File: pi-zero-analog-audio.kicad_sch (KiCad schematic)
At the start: 25 parts, among them J1 GPIO, J2 SJ1-3555NG-BE, J3 Screw_Terminal_01x04, U1 LP5907MFX-3.3, U2 74LVC2G34, U3 PAM8403D

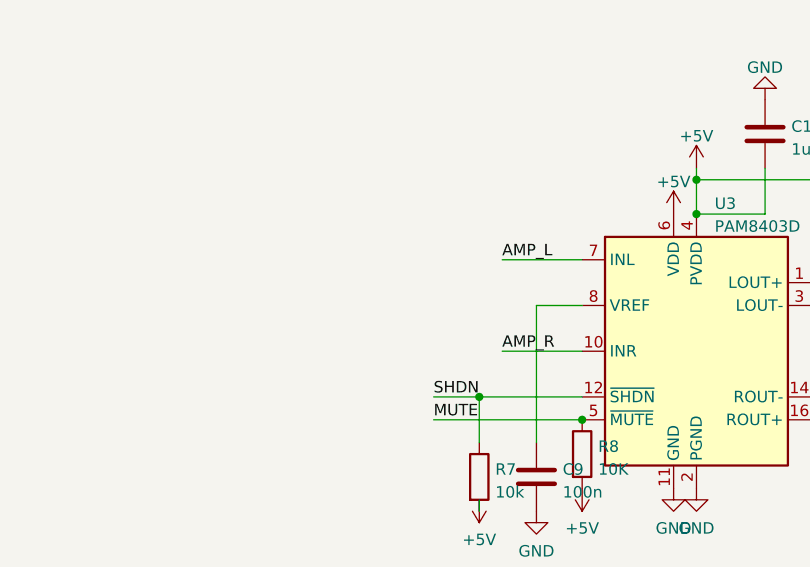
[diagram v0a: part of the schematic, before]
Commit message: Capacitor and resistor on the amplifier input, as per PAM8403 specs
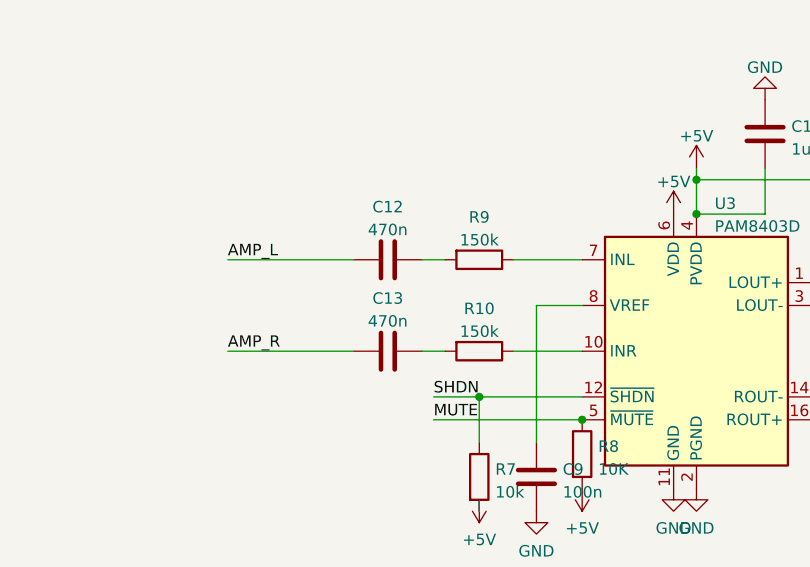
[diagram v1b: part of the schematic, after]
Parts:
- added C12, C13: 470n, Capacitor_SMD:C_0805_2012Metric_Pad1.18x1.45mm_HandSolder, symbol Device:C
- added R10, R9: 150k, Resistor_SMD:R_0805_2012Metric_Pad1.20x1.40mm_HandSolder, symbol Device:R
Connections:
- net AMP_L: now also C12.2; no longer U3.7 (INL)
- net AMP_R: now also C13.2; no longer U3.10 (INR)
- new net: R10.1, U3.10 (INR)
- new net: R9.1, U3.7 (INL)
- new net: C12.1, R9.2
- new net: C13.1, R10.2
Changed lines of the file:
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@@
+    (stroke (width 0) (type default) (color 0 0 0 0))
+  )
+  (wire (pts (xy 97.79 107.95) (xy 100.33 107.95))
     (stroke (width 0) (type default) (color 0 0 0 0))
   )
@@
     (stroke (width 0) (type default) (color 0 0 0 0))
   )
+  (wire (pts (xy 76.2 118.11) (xy 90.17 118.11))
+    (stroke (width 0) (type default) (color 0 0 0 0))
+  )
   (wire (pts (xy 40.64 64.77) (xy 38.1 64.77))
     (stroke (width 0) (type solid) (color 0 0 0 0))
@@
     (stroke (width 0) (type default) (color 0 0 0 0))
   )
+  (wire (pts (xy 97.79 118.11) (xy 100.33 118.11))
+    (stroke (width 0) (type default) (color 0 0 0 0))
+  )
   (wire (pts (xy 40.64 26.67) (xy 38.1 26.67))
     (stroke (width 0) (type solid) (color 0 0 0 0))
@@
     (stroke (width 0) (type default) (color 0 0 0 0))
   )
-  (wire (pts (xy 106.68 118.11) (xy 115.57 118.11))
+  (wire (pts (xy 107.95 118.11) (xy 115.57 118.11))
     (stroke (width 0) (type default) (color 0 0 0 0))
   )
@@
     (stroke (width 0) (type default) (color 0 0 0 0))
   )
-  (wire (pts (xy 106.68 107.95) (xy 115.57 107.95))
+  (wire (pts (xy 76.2 107.95) (xy 90.17 107.95))
     (stroke (width 0) (type default) (color 0 0 0 0))
   )
   (wire (pts (xy 15.24 64.77) (xy 25.4 64.77))
+    (stroke (width 0) (type default) (color 0 0 0 0))
+  )
+  (wire (pts (xy 107.95 107.95) (xy 115.57 107.95))
     (stroke (width 0) (type default) (color 0 0 0 0))
   )
@@
     (effects (font (size 1.27 1.27)) (justify left bottom))
   )
-  (label "AMP_L" (at 106.68 107.95 0)
+  (label "AMP_L" (at 76.2 107.95 0)
     (effects (font (size 1.27 1.27)) (justify left bottom))
   )
@@
     (effects (font (size 1.27 1.27)) (justify left bottom))
   )
-  (label "AMP_R" (at 106.68 118.11 0)
+  (label "AMP_R" (at 76.2 118.11 0)
     (effects (font (size 1.27 1.27)) (justify left bottom))
   )
@@
     (pin "1")
   )
+  (symbol (lib_id "Device:C") (at 93.98 107.95 270) (unit 1)
+    (in_bom yes) (on_board yes) (fields_autoplaced)
+    (property "Reference" "C12" (id 0) (at 93.98 102.0912 90))
+    (property "Value" "470n" (id 1) (at 93.98 104.6281 90))
+    (property "Footprint" "Capacitor_SMD:C_0805_2012Metric_Pad1.18x1.45mm_HandSolder" (id 2) (at 90.17 108.9152 0)
+      (effects (font (size 1.27 1.27)) hide)
+    )
+    (property "Datasheet" "~" (id 3) (at 93.98 107.95 0)
+      (effects (font (size 1.27 1.27)) hide)
+    )
+    (pin "1")
+    (pin "2")
+  )
   (symbol (lib_id "Device:C") (at 138.43 55.88 0) (unit 1)
     (in_bom yes) (on_board yes) (fields_autoplaced)
@@
     (pin "4")
   )
+  (symbol (lib_id "Device:C") (at 93.98 118.11 270) (unit 1)
+    (in_bom yes) (on_board yes) (fields_autoplaced)
+    (property "Reference" "C13" (id 0) (at 93.98 112.2512 90))
+    (property "Value" "470n" (id 1) (at 93.98 114.7881 90))
+    (property "Footprint" "Capacitor_SMD:C_0805_2012Metric_Pad1.18x1.45mm_HandSolder" (id 2) (at 90.17 119.0752 0)
+      (effects (font (size 1.27 1.27)) hide)
+    )
+    (property "Datasheet" "~" (id 3) (at 93.98 118.11 0)
+      (effects (font (size 1.27 1.27)) hide)
+    )
+    (pin "1")
+    (pin "2")
+  )
   (symbol (lib_id "power:GND") (at 128.27 133.35 0) (unit 1)
     (in_bom yes) (on_board yes) (fields_autoplaced)
@@
     (pin "1")
   )
+  (symbol (lib_id "Device:R") (at 104.14 118.11 270) (unit 1)
+    (in_bom yes) (on_board yes) (fields_autoplaced)
+    (property "Reference" "R10" (id 0) (at 104.14 113.3942 90))
+    (property "Value" "150k" (id 1) (at 104.14 115.9311 90))
+    (property "Footprint" "Resistor_SMD:R_0805_2012Metric_Pad1.20x1.40mm_HandSolder" (id 2) (at 104.14 116.332 90)
+      (effects (font (size 1.27 1.27)) hide)
+    )
+    (property "Datasheet" "~" (id 3) (at 104.14 118.11 0)
+      (effects (font (size 1.27 1.27)) hide)
+    )
+    (pin "1")
+    (pin "2")
+  )
   (symbol (lib_id "Device:R") (at 115.57 129.54 0) (unit 1)
     (in_bom yes) (on_board yes) (fields_autoplaced)
@@
     )
     (property "Datasheet" "~" (id 3) (at 121.92 34.29 0)
+      (effects (font (size 1.27 1.27)) hide)
+    )
+    (pin "1")
+    (pin "2")
+  )
+  (symbol (lib_id "Device:R") (at 104.14 107.95 270) (unit 1)
+    (in_bom yes) (on_board yes) (fields_autoplaced)
+    (property "Reference" "R9" (id 0) (at 104.14 103.2342 90))
+    (property "Value" "150k" (id 1) (at 104.14 105.7711 90))
+    (property "Footprint" "Resistor_SMD:R_0805_2012Metric_Pad1.20x1.40mm_HandSolder" (id 2) (at 104.14 106.172 90)
+      (effects (font (size 1.27 1.27)) hide)
+    )
+    (property "Datasheet" "~" (id 3) (at 104.14 107.95 0)
       (effects (font (size 1.27 1.27)) hide)
     )
@@
       (reference "C11") (unit 1) (value "1u") (footprint "Capacitor_SMD:C_0805_2012Metric_Pad1.18x1.45mm_HandSolder")
     )
+    (path "/201c8162-e217-46e1-ac40-c57d7147d95c"
+      (reference "C12") (unit 1) (value "470n") (footprint "Capacitor_SMD:C_0805_2012Metric_Pad1.18x1.45mm_HandSolder")
+    )
+    (path "/49164358-7523-45d6-8e05-0933751a598b"
+      (reference "C13") (unit 1) (value "470n") (footprint "Capacitor_SMD:C_0805_2012Metric_Pad1.18x1.45mm_HandSolder")
+    )
     (path "/00000000-0000-0000-0000-000059ad464a"
       (reference "J1") (unit 1) (value "GPIO") (footprint "Connector_PinSocket_2.54mm:PinSocket_2x20_P2.54mm_Vertical")
@@
       (reference "R8") (unit 1) (value "10K") (footprint "Resistor_SMD:R_0805_2012Metric_Pad1.20x1.40mm_HandSolder")
     )
+    (path "/d084b509-2bd2-4510-bb62-a6e63bec94c3"
+      (reference "R9") (unit 1) (value "150k") (footprint "Resistor_SMD:R_0805_2012Metric_Pad1.20x1.40mm_HandSolder")
+    )
+    (path "/a56b6fb7-621d-4fc3-8ca0-7aa63cd0dea4"
+      (reference "R10") (unit 1) (value "150k") (footprint "Resistor_SMD:R_0805_2012Metric_Pad1.20x1.40mm_HandSolder")
+    )
     (path "/ece134dc-481d-4acc-afc4-a752a7a1b75d"

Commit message: The resistor should be max 142k as per specs
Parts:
- R10, R9: value 150k -> 140k
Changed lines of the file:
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@@
     (in_bom yes) (on_board yes) (fields_autoplaced)
     (property "Reference" "R10" (id 0) (at 104.14 113.3942 90))
-    (property "Value" "150k" (id 1) (at 104.14 115.9311 90))
+    (property "Value" "140k" (id 1) (at 104.14 115.9311 90))
     (property "Footprint" "Resistor_SMD:R_0805_2012Metric_Pad1.20x1.40mm_HandSolder" (id 2) (at 104.14 116.332 90)
       (effects (font (size 1.27 1.27)) hide)
@@
     (in_bom yes) (on_board yes) (fields_autoplaced)
     (property "Reference" "R9" (id 0) (at 104.14 103.2342 90))
-    (property "Value" "150k" (id 1) (at 104.14 105.7711 90))
+    (property "Value" "140k" (id 1) (at 104.14 105.7711 90))
     (property "Footprint" "Resistor_SMD:R_0805_2012Metric_Pad1.20x1.40mm_HandSolder" (id 2) (at 104.14 106.172 90)
       (effects (font (size 1.27 1.27)) hide)
@@
     )
     (path "/d084b509-2bd2-4510-bb62-a6e63bec94c3"
-      (reference "R9") (unit 1) (value "150k") (footprint "Resistor_SMD:R_0805_2012Metric_Pad1.20x1.40mm_HandSolder")
+      (reference "R9") (unit 1) (value "140k") (footprint "Resistor_SMD:R_0805_2012Metric_Pad1.20x1.40mm_HandSolder")
     )
     (path "/a56b6fb7-621d-4fc3-8ca0-7aa63cd0dea4"
-      (reference "R10") (unit 1) (value "150k") (footprint "Resistor_SMD:R_0805_2012Metric_Pad1.20x1.40mm_HandSolder")
+      (reference "R10") (unit 1) (value "140k") (footprint "Resistor_SMD:R_0805_2012Metric_Pad1.20x1.40mm_HandSolder")
     )
     (path "/ece134dc-481d-4acc-afc4-a752a7a1b75d"

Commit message: Some footprint changes
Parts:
- U1: footprint Package_TO_SOT_SMD:SOT-23-5 -> Package_TO_SOT_SMD:SOT-23-5_HandSoldering
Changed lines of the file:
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@@
     (property "Reference" "U1" (id 0) (at 68.58 24.2402 0))
     (property "Value" "LP5907MFX-3.3" (id 1) (at 68.58 26.7771 0))
-    (property "Footprint" "Package_TO_SOT_SMD:SOT-23-5" (id 2) (at 68.58 24.13 0)
+    (property "Footprint" "Package_TO_SOT_SMD:SOT-23-5_HandSoldering" (id 2) (at 68.58 24.13 0)
       (effects (font (size 1.27 1.27)) hide)
     )
@@
     )
     (path "/ece134dc-481d-4acc-afc4-a752a7a1b75d"
-      (reference "U1") (unit 1) (value "LP5907MFX-3.3") (footprint "Package_TO_SOT_SMD:SOT-23-5")
+      (reference "U1") (unit 1) (value "LP5907MFX-3.3") (footprint "Package_TO_SOT_SMD:SOT-23-5_HandSoldering")
     )
     (path "/0d4d57aa-e3d3-44e9-8952-39267bfe2073"

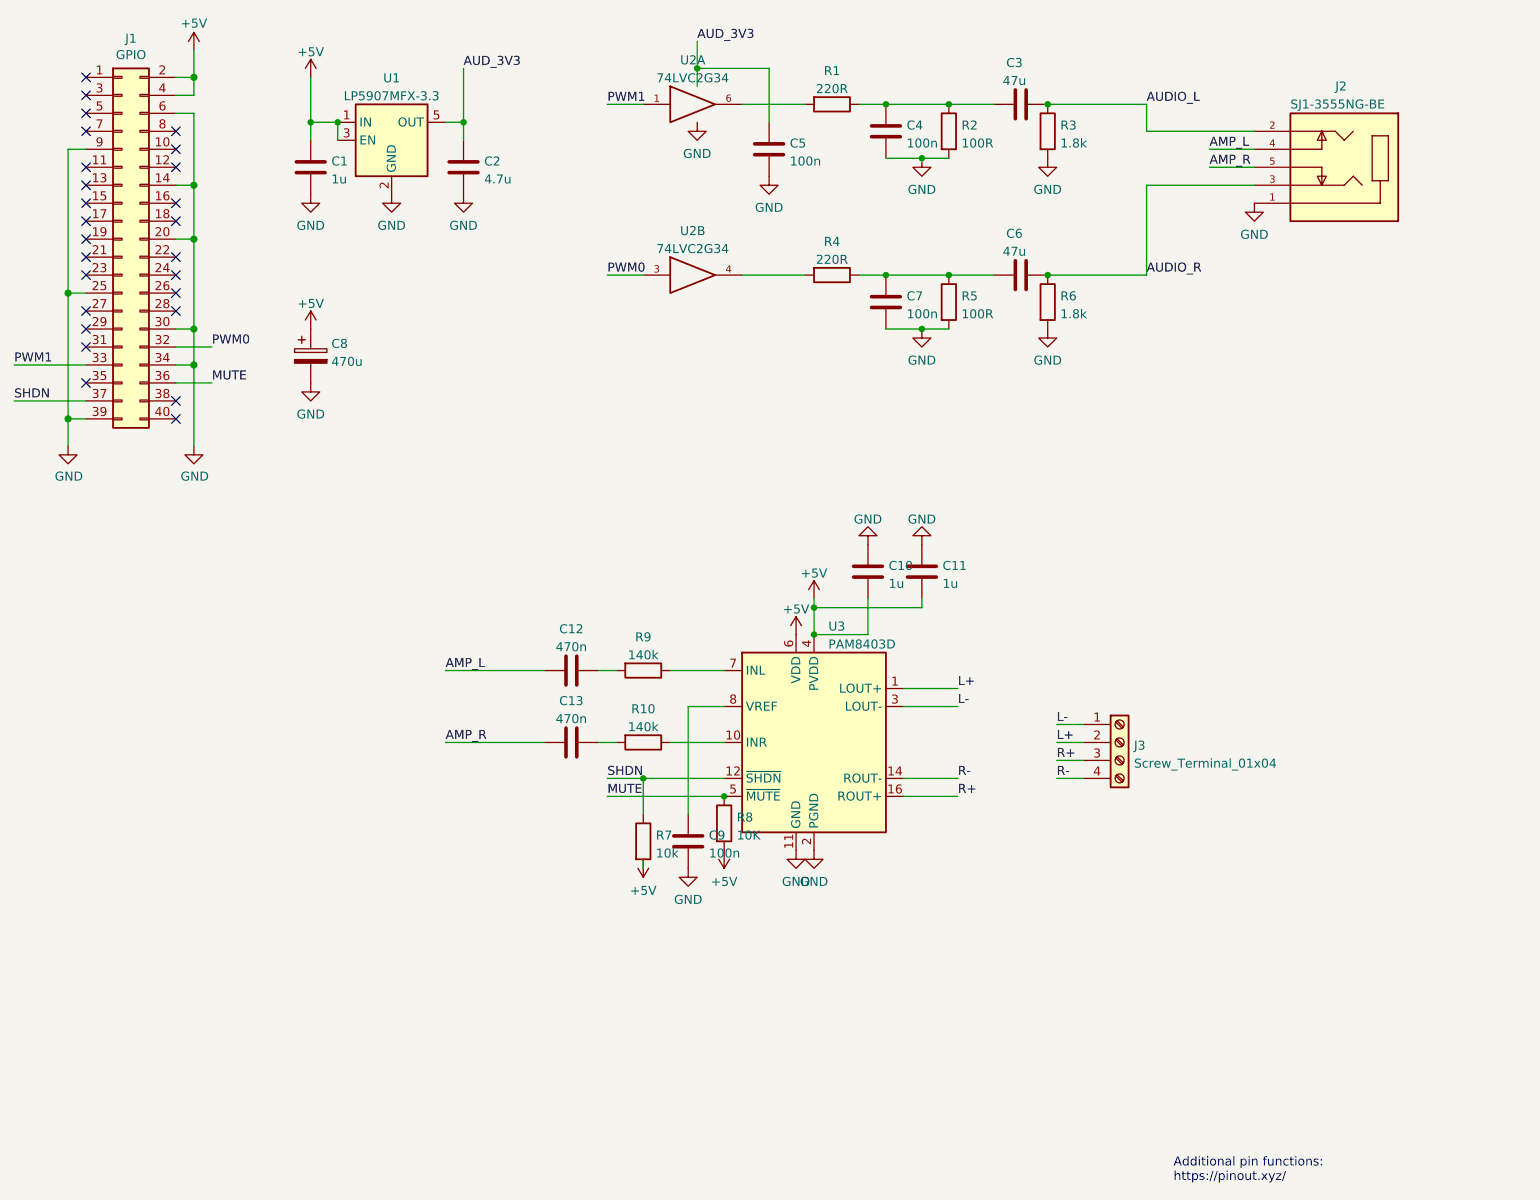
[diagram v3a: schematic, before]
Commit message: rewrite to components that I actually can have
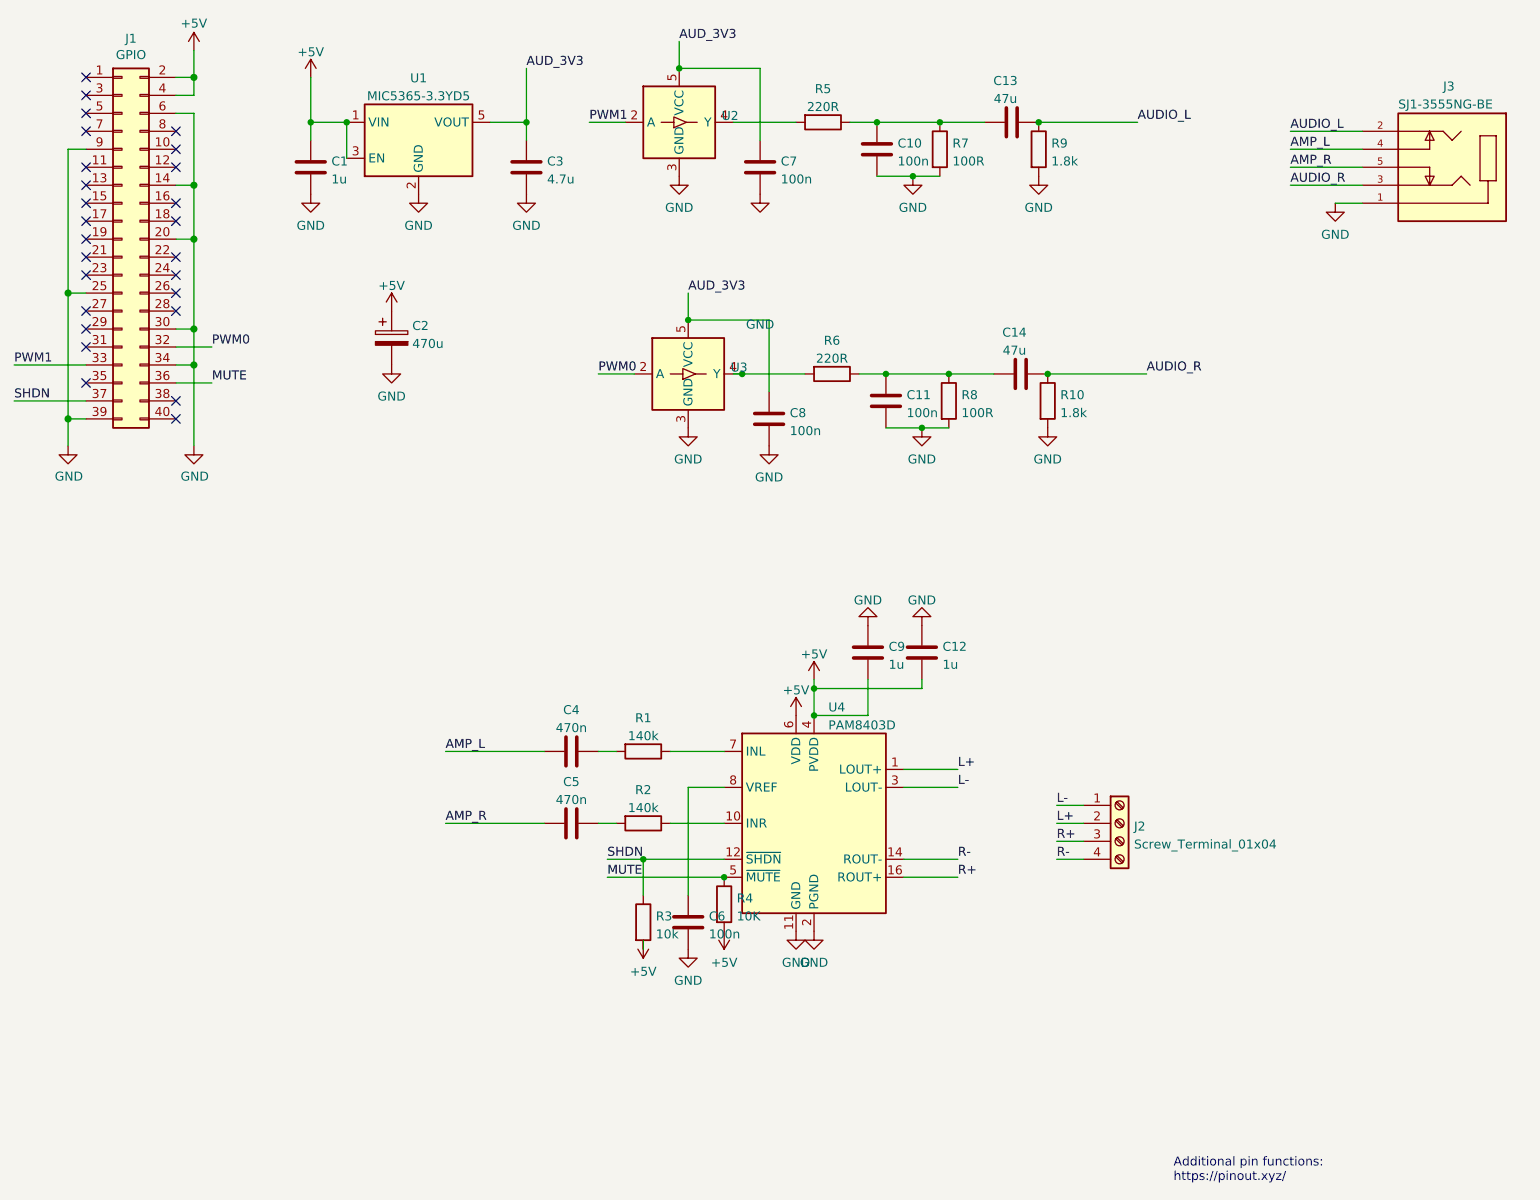
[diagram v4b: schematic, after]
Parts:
- removed U1: LP5907MFX-3.3, Package_TO_SOT_SMD:SOT-23-5_HandSoldering, symbol Regulator_Linear:LP5907MFX-3.3
- removed U2: 74LVC2G34, Package_TO_SOT_SMD:SOT-23-6_Handsoldering, symbol 74xGxx:74LVC2G34
- added C8: 100n, Capacitor_SMD:C_0805_2012Metric_Pad1.18x1.45mm_HandSolder, symbol Device:C
- added U1: MIC5365-3.3YD5, Package_TO_SOT_SMD:SOT-23-5, symbol Regulator_Linear:MIC5365-3.3YD5
- added U2, U3: MC74VHC1GT50, Package_TO_SOT_SMD:SOT-23-5_HandSoldering, symbol Logic_LevelTranslator:SN74LV1T34DBV
- renumbered C4 to C10, C7 to C11, C11 to C12, C3 to C13, C6 to C14, C8 to C2, C2 to C3, C12 to C4, C13 to C5, C9 to C6, C5 to C7, C10 to C9, J3 to J2, J2 to J3, R9 to R1, R6 to R10, R10 to R2, R7 to R3, R8 to R4, R1 to R5, R4 to R6, R2 to R7, R5 to R8, R3 to R9, U3 to U4
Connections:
- net +5V: now also U1.1 (VIN), U1.3 (EN)
- net GND: now also C8.2, U1.2 (GND), U2.3 (GND), U3.3 (GND)
- net PWM0: now also U3.2 (A)
- net PWM1: now also U2.2 (A)
- net at R5.2: now also U2.4 (Y)
- net at R6.2: now also U3.4 (Y)
- net VCC renamed AUD_3V3
- net AUD_3V3: now also C8.1, U1.5 (VOUT), U2.5 (VCC), U3.5 (VCC)
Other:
- moved on the sheet: C10, C11, C12, C13, C14, C2, C3, C4, C5, C6, C7, C9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
